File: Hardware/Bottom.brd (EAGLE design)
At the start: 120 x 80 mm, 91 parts, among them IC1 SI570, IC2 74LVC74A, IC3 74LVC1G17DCK, IC5 LT6232CGN, Q1 DMPH6050SK3

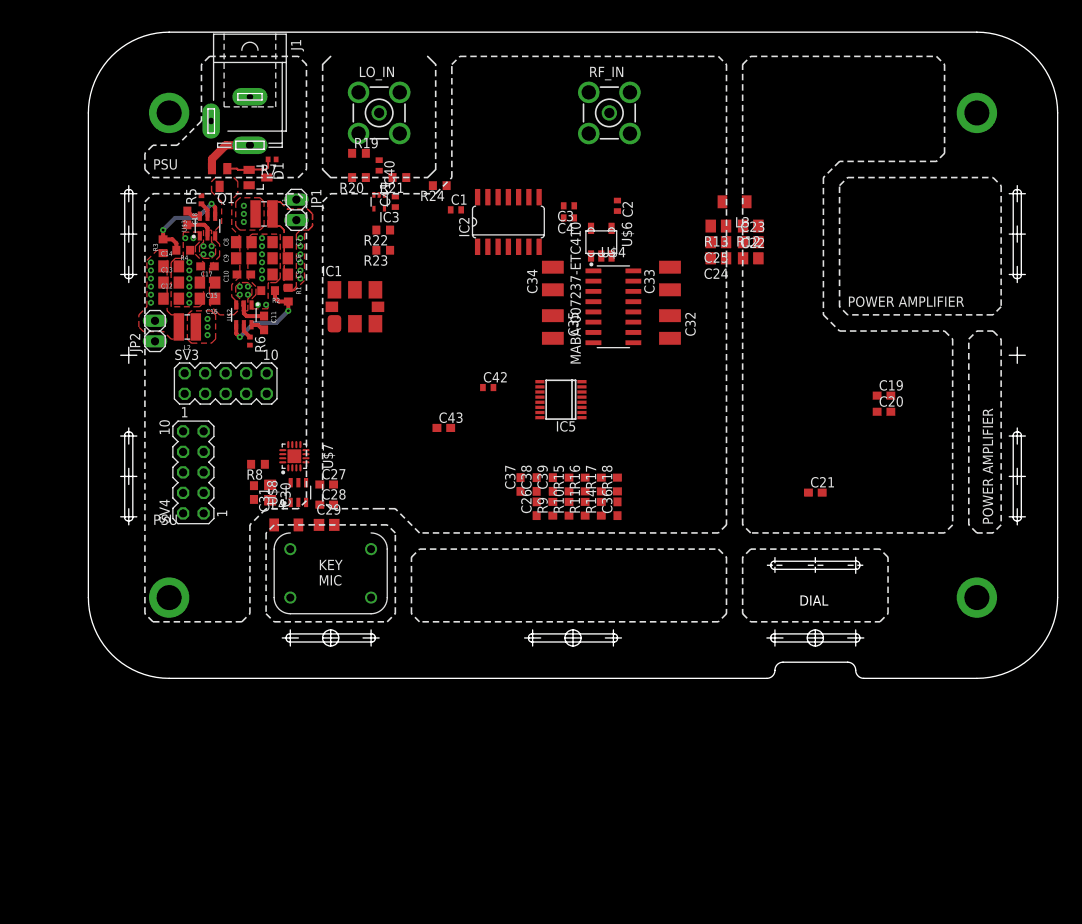
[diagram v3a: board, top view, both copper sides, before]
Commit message: Advance layout bottom
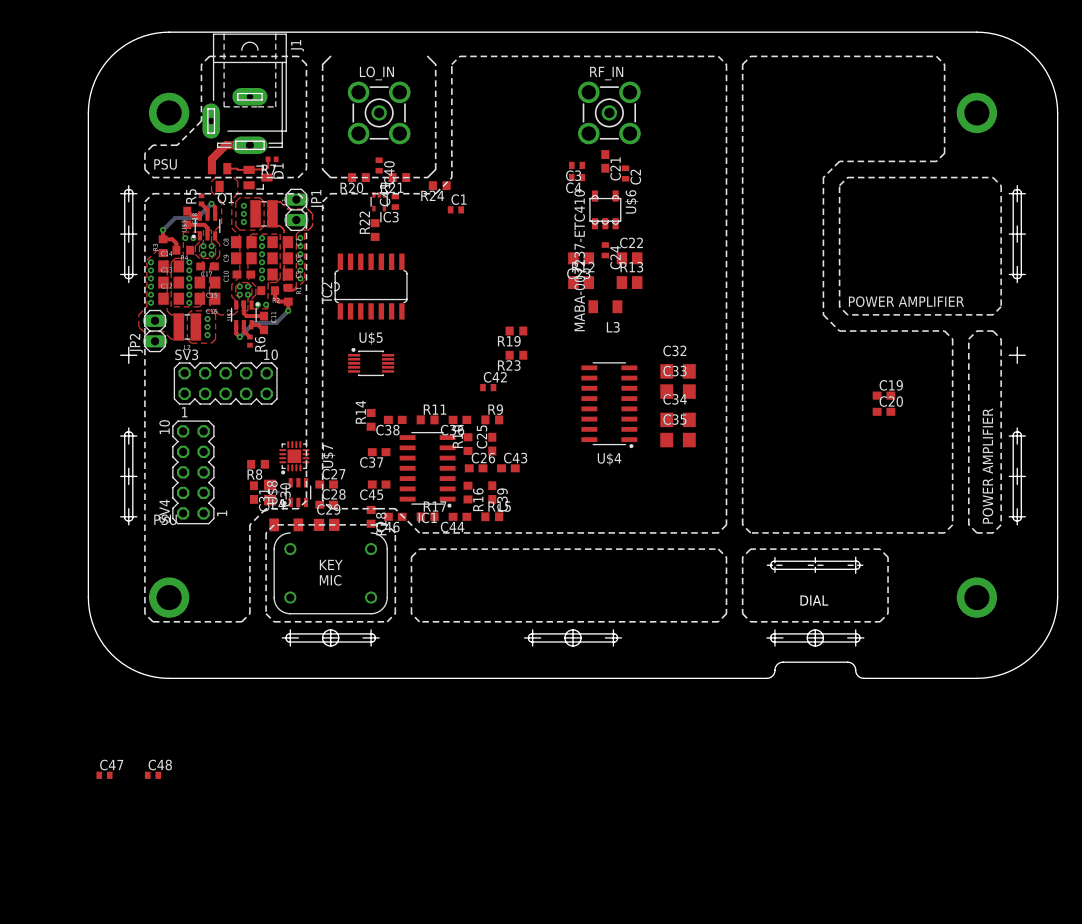
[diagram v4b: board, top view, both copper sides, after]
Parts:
- removed IC5: LT6232CGN, linear-technology:SSOP16
- added C44: 680p, rcl:C0603
- added C45: 22p, rcl:C0603
- added C46: 470p, rcl:C0603
- added C47: 100n, rcl:C0402
- added C48: 10n, rcl:C0402
- added U$5: SI5351A-B-GTMSOP10, MyLib:SOP50P490X110-10
- C24: device rcl:C0805 -> rcl:C0402
- C25: value 4µ7 -> 68p; device rcl:C0805 -> rcl:C0603
- C32, C33, C34, C35: device rcl:C1210 -> rcl:C1206
- C36: value (none) -> 680p
- C37: value (none) -> 22p
- C38: value (none) -> 470p
- C39: value (none) -> 68p
- IC1: value SI570 -> OP491SOIC_N14; device silabs:8-PIN -> MyLib:SOIC127P600X155-14
- IC2: value 74LVC74A -> (none)
- R10, R16: value (none) -> 150k
- R11, R14, R17, R18: value (none) -> 47k
- R15, R9: value (none) -> 6k8
- R19: value 47R -> DNP
- moved C21 48.5 mm to (64.0, 64.0), turned to 270 degrees
- moved C25 37.5 mm to (50.0, 29.0), turned to 90 degrees
- moved R18 30.8 mm to (35.0, 20.0), turned to 270 degrees
- moved R14 30.5 mm to (35.0, 32.0)
- moved R19 29.4 mm to (53.0, 43.0), turned to 180 degrees
- moved C34 23.4 mm to (73.0, 32.0), turned to 0 degrees
- moved C36 22.4 mm to (46.0, 32.0), turned to 180 degrees
- moved R11 22.4 mm to (42.0, 32.0), turned to 0 degrees
- moved R12 22.1 mm to (61.0, 49.0), turned to 0 degrees
- moved IC1 21.9 mm to (42.0, 26.0), turned to 180 degrees
- moved R17 21.9 mm to (42.0, 20.0), turned to 0 degrees
- moved C23 21.1 mm to (61.0, 52.0), turned to 180 degrees
- moved R23 21.0 mm to (53.0, 40.0)
- moved C35 20.9 mm to (73.0, 29.5), turned to 0 degrees
- moved L3 20.6 mm to (64.0, 46.0)
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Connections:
- removed net I2C_OSC_SCL: IC1.8
- removed net I2C_OSC_SDA: IC1.7
- removed net N$22: U$4.2
- removed net N$40: C38.1, R10.1, R9.2
- removed net N$45: IC5.11, R17.2, R18.2
- removed net N$59: C34.1, IC5.2, U$4.10, U$4.4
- removed net V+: U$4.16
- removed net V-: U$4.8
- new net BASEBAND_I: C46.2, IC1.13, IC1.14
- new net BASEBAND_Q: C38.2, IC1.8, IC1.9
- new net CLK_I: IC2.5, R19.1, U$4.14
- new net CLK_Q: IC2.8, R23.1, U$4.2
- new net N$34: C35.1, U$4.11, U$4.3
- new net N$53: C33.1, U$4.13, U$4.5
- new net N$54: C45.1, IC1.12, R18.1
- net +3V3: now also C47.1, C48.1, L3.2, SV3.6, SV3.8, U$4.16, U$5.1, U$5.7; no longer IC1.6, R13.2
- net +5V: now also IC1.4; no longer IC5.4
- net GND: now also C39.2, C45.2, C47.2, C48.2, IC1.11, U$4.8, U$5.8; no longer C36.2, IC1.3, IC5.13, R15.1, R17.1, R19.1
- net I2C_MCS_SCL: now also SV3.10, U$5.4; no longer SV3.9
- net I2C_MCS_SDA: now also SV3.9, U$5.5; no longer SV3.10
- net N$1: now also R19.2, U$5.10; no longer IC2.5
- net N$10: now also C36.1, R10.2, R9.1; no longer C39.1, R11.2, R14.1
- net N$13: now also C25.1, IC1.5, R10.1; no longer C37.1, IC5.14, R14.2
- net N$14: now also C36.2, IC1.6, IC1.7, R11.2; no longer IC5.1, R9.1
- net N$18: now also R13.1; no longer C25.1, L3.1
- net N$2: no longer R23.1
- net N$21: now also L3.1, R13.2; no longer L3.2, R13.1
- net N$23: now also C34.1, U$4.10, U$4.4; no longer U$4.14
- net N$24: no longer IC5.3
- net N$33: now also C38.1, R11.1, R14.2; no longer C33.1, IC5.5, U$4.13, U$4.5
- net N$39: now also C37.1, IC1.10, R14.1; no longer C35.1, IC5.6, U$4.11, U$4.3
- net N$41: now also R15.2; no longer C36.1, IC5.12, R10.2
- net N$42: now also C44.1, R15.1, R16.2; no longer C38.2, IC5.10, R18.1
- net N$43: now also C39.1, IC1.3; no longer C39.2, IC5.16
- net N$44: now also C44.2, IC1.1, IC1.2, R17.2; no longer IC5.15, R15.2, R16.2
- net N$46: no longer R19.2
- net N$5: now also R23.2, U$5.9; no longer IC2.8
- net N$50: now also C46.1, R17.1, R18.2; no longer IC1.4, R23.2
- net N$6: now also R9.2; no longer IC5.7, R11.1

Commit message: Add RF Buffer
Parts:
- removed U$4: SN74CBT3253SOIC16, MyLib:SOIC127P600X175-16
- added C49: 100n, rcl:C0402
- added C50: 10n, rcl:C0402
- added IC4: LT6231, MyLib:SO8
- added IC5: SN74CBT3253SOIC16, MyLib:SOIC127P600X175-16
- added Q2: 25MHz, MyLib:ABM10W
- added R25, R26, R27, R28, R29, R30: 100R, rcl:R0603
- moved C2 37.0 mm to (35.0, 43.0), turned to 0 degrees
- moved C1 19.6 mm to (35.0, 41.5)
- moved C32 12.7 mm to (82.0, 47.0)
- moved C33 12.7 mm to (82.0, 44.5)
- moved C34 12.7 mm to (82.0, 41.0)
- moved C35 12.7 mm to (82.0, 38.5)
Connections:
- new net N$22: IC4.3, R25.1
- new net N$40: IC4.2, R26.1, R29.2
- new net N$45: IC4.5, R27.1
- new net N$55: IC4.6, R28.1, R30.2
- new net N$56: Q2.4, U$5.2
- new net N$57: IC4.1, R15.2, R29.1
- net +3V3: now also C26.1, C43.1, C49.1, C50.1, IC1.4, IC4.8, IC5.16; no longer U$4.16
- net +5V: no longer C26.1, C43.1, IC1.4
- net CLK_I: now also IC5.14; no longer U$4.14
- net CLK_Q: now also IC5.2; no longer U$4.2
- net GND: now also C49.2, C50.2, IC4.4, IC5.1, IC5.15, IC5.8; no longer U$4.1, U$4.15, U$4.8
- net N$23: now also IC5.10, IC5.4, R27.2; no longer U$4.10, U$4.4
- net N$24: now also IC5.12, IC5.6, R25.2; no longer U$4.12, U$4.6
- net N$34: now also IC5.11, IC5.3, R28.2; no longer U$4.11, U$4.3
- net N$41: now also Q2.1, U$5.3; no longer R15.2
- net N$51: now also IC5.9; no longer U$4.9
- net N$52: now also IC5.7; no longer U$4.7
- net N$53: now also IC5.13, IC5.5, R26.2; no longer U$4.13, U$4.5
- net N$6: now also IC4.7, R30.1

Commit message: Add various parts
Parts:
- added BB_I, BB_Q: BU-SMA-V, con-coax:BU-SMA-V
- added JP3: (no value), pinhead:2X03
- added R31, R32: DNP, rcl:R0603
- moved C47 89.9 mm to (53.0, 62.0), turned to 90 degrees
- moved C48 85.8 mm to (51.5, 62.0), turned to 90 degrees
- moved C49 81.8 mm to (47.5, 42.0), turned to 270 degrees
- moved C50 78.3 mm to (43.0, 44.0), turned to 270 degrees
- moved C35 30.4 mm to (53.0, 47.5), turned to 270 degrees
- moved C19 27.7 mm to (71.8, 42.6)
- moved C20 27.4 mm to (71.8, 39.4)
- moved C34 26.8 mm to (56.0, 47.5), turned to 270 degrees
- moved C3 24.1 mm to (44.5, 45.5), turned to 270 degrees
- moved R12 23.9 mm to (56.5, 72.5)
- moved C33 23.2 mm to (59.0, 47.5), turned to 270 degrees
- moved C4 22.0 mm to (46.0, 45.5), turned to 270 degrees
- moved C32 20.0 mm to (62.0, 47.5), turned to 270 degrees
- moved IC5 19.9 mm to (57.5, 55.5), turned to 90 degrees
- moved R13 19.1 mm to (56.5, 65.0), turned to 180 degrees
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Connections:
- removed net N$25: U$7.8
- removed net N$28: U$7.6
- new net N$58: IC2.8, R32.2
- new net N$59: IC2.5, R31.2
- net BASEBAND_I: now also BB_I.1, JP3.2
- net BASEBAND_Q: now also BB_Q.1, JP3.6
- net CLK_I: now also R31.1; no longer IC2.5
- net CLK_Q: now also R32.1; no longer IC2.8
- net GND: now also BB_I.2, BB_I.3, BB_I.4, BB_I.5, BB_Q.2, BB_Q.3, BB_Q.4, BB_Q.5, JP3.3, JP3.4, U$7.6, U$7.7
- net N$26: now also JP3.1, U$7.8; no longer U$7.7
- net N$32: now also JP3.5
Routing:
- net BASEBAND_I: track 0.00 -> 24.2 mm, vias 0 -> 1
- net N$34: track 0.00 -> 24.2 mm, vias 0 -> 2
- net N$23: track 0.00 -> 23.5 mm, vias 0 -> 2
- net N$57: track 0.00 -> 21.6 mm
- net N$29: track 0.00 -> 20.0 mm
- net GND: track 0.00 -> 19.9 mm, vias 16 -> 25
- net N$24: track 0.00 -> 19.8 mm
- net N$53: track 0.00 -> 19.0 mm
- net N$18: track 0.00 -> 17.0 mm, vias 0 -> 1
- net +3V3: track 0.00 -> 12.8 mm, vias 0 -> 3
- net BASEBAND_Q: track 0.00 -> 11.1 mm, vias 0 -> 1
- net N$47: track 0.00 -> 10.1 mm
- net N$40: track 0.00 -> 9.32 mm
- net N$6: track 0.00 -> 7.41 mm
- net N$55: track 0.00 -> 7.06 mm
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
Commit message: Add various parts
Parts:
- removed C42: 10n, rcl:C0402
- removed C43: 1u, rcl:C0603
- moved C3 18.5 mm to (45.5, 64.0), turned to 180 degrees
- moved C50 17.3 mm to (55.5, 32.0), turned to 0 degrees
- moved C4 17.0 mm to (45.5, 62.5), turned to 180 degrees
- moved C49 14.0 mm to (55.5, 30.5), turned to 0 degrees
- moved C47 5.41 mm to (50.0, 57.5), turned to 270 degrees
- moved C48 4.50 mm to (51.5, 57.5), turned to 270 degrees
- moved R19 4.03 mm to (40.5, 51.0)
- moved R23 4.03 mm to (40.5, 48.5)
- moved R31 2.24 mm to (44.5, 51.0), turned to 0 degrees
- moved R32 1.58 mm to (44.5, 48.5), turned to 0 degrees
- moved C1 1.50 mm to (34.3, 51.5)
- moved C2 1.50 mm to (35.4, 51.5)
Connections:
- net +3V3: no longer C42.1, C43.1
- net GND: no longer C42.2, C43.2
- net I2C_MCS_SCL: now also SV3.9; no longer SV3.10
- net I2C_MCS_SDA: now also SV3.10; no longer SV3.9
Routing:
- net I2C_MCS_SCL: track 0.00 -> 22.5 mm
- net I2C_MCS_SDA: track 0.00 -> 20.6 mm
- net +3V3: track 12.8 -> 30.6 mm, vias 3 -> 10
- net CLK_Q: track 3.61 -> 17.5 mm, vias 0 -> 2
- net CLK_I: track 4.72 -> 17.9 mm, vias 0 -> 2
- net N$51: track 0.00 -> 13.0 mm
- net BASEBAND_I: track 24.2 -> 37.1 mm
- net BASEBAND_Q: track 11.1 -> 22.6 mm
- net N$4: track 0.00 -> 10.0 mm, vias 0 -> 2
- net N$3: track 0.00 -> 9.86 mm, vias 0 -> 2
- net N$5: track 0.00 -> 9.08 mm
- net VDD_DC: track 0.00 -> 8.41 mm
- net N$52: track 6.52 -> 14.8 mm
- net N$59: track 0.00 -> 8.06 mm
- net N$1: track 0.00 -> 7.94 mm
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
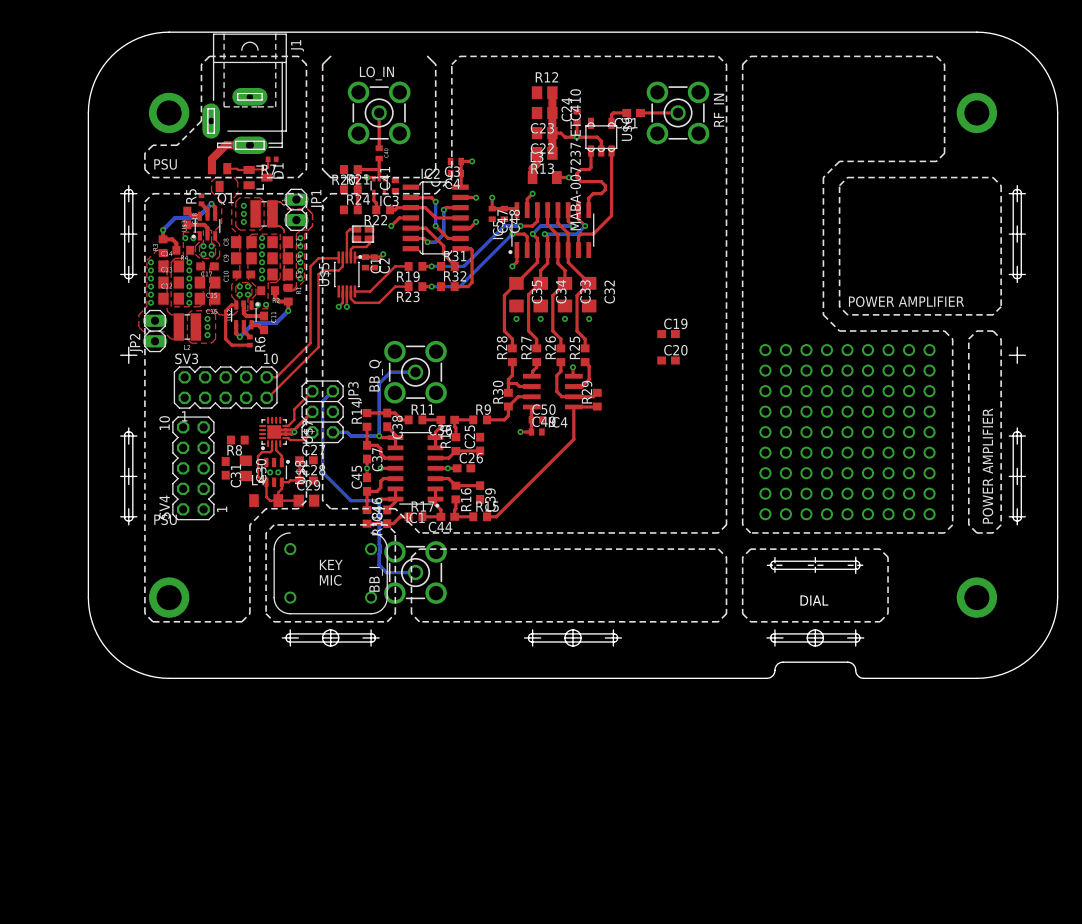
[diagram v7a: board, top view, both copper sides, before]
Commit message: Advance layout bottom
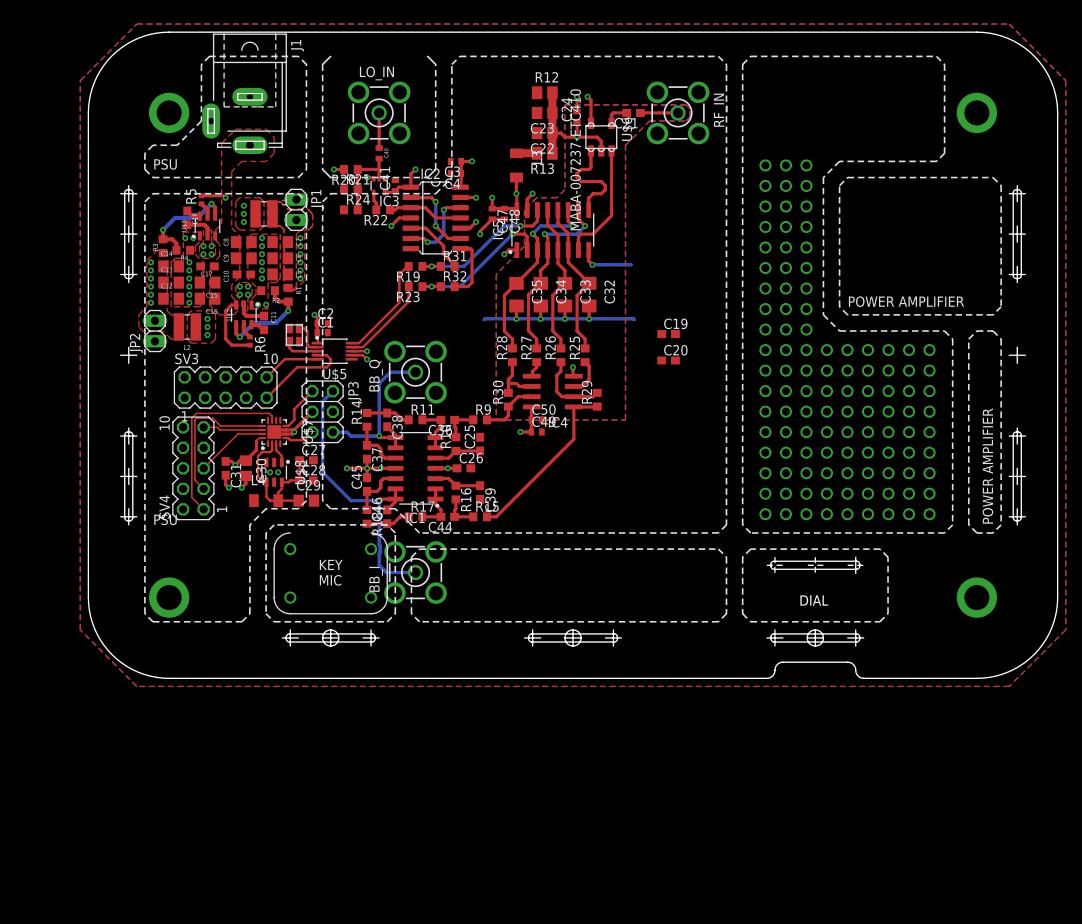
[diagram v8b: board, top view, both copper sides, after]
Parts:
- removed D1: 10V, diode:SOT23
- removed Q1: DMPH6050SK3, MyLib:SOT23
- removed R7: 100k, rcl:R0402
- removed R8: 10k, rcl:R0603
- moved Q2 15.1 mm to (25.5, 42.5), turned to 90 degrees
- moved C1 10.2 mm to (29.0, 42.8), turned to 0 degrees
- moved C2 9.94 mm to (29.0, 43.9), turned to 0 degrees
- moved U$5 9.62 mm to (30.5, 40.5), turned to 0 degrees
- moved L3 3.81 mm to (53.0, 63.5), turned to 270 degrees
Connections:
- removed net N$12: J1.3, Q1.2
- removed net N$9: D1.1, Q1.1, R7.2
- removed net SPI_ADC_MISO: R8.1, U$7.15
- net GND: no longer R7.1
- net SPI_MCS_MISO: now also U$7.15; no longer R8.2
- net VDD_DC: now also J1.3; no longer D1.3, Q1.3
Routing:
- net GND: track 21.8 -> 70.1 mm, vias 26 -> 37
- net ADC_CHSEL: track 0.00 -> 22.7 mm
- net SPI_MCS_CS: track 0.00 -> 17.8 mm
- net +3V3: track 30.6 -> 47.4 mm, vias 10 -> 13
- net I2C_MCS_SDA: track 20.6 -> 7.24 mm
- net I2C_MCS_SCL: track 22.5 -> 12.0 mm
- net SPI_MCS_MISO: track 0.00 -> 9.05 mm
- net SPI_MCS_CLK: track 0.00 -> 7.43 mm
- net N$12: track 6.60 -> 0.00 mm
- net N$9: track 6.24 -> 0.00 mm
- net N$1: track 7.94 -> 13.0 mm
- net VDD_DC: track 8.41 -> 11.5 mm, vias 0 -> 1
- net N$5: track 9.08 -> 11.2 mm
- net CLK_Q: track 17.5 -> 18.6 mm
- net CLK_I: track 17.9 -> 19.1 mm
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- added copper zone on layer 15, net +3V3
- added copper zone on layer 1, net CUTOUT
- added copper zone on layer 15, net CUTOUT
- added copper zone on layer 16, net CUTOUT
- added copper zone on layer 2, net CUTOUT
- added copper zone on layer 16, net GND
